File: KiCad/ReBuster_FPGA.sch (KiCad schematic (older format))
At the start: 28 parts, among them U1 10M02SCU169, U2 LM1117-3.3

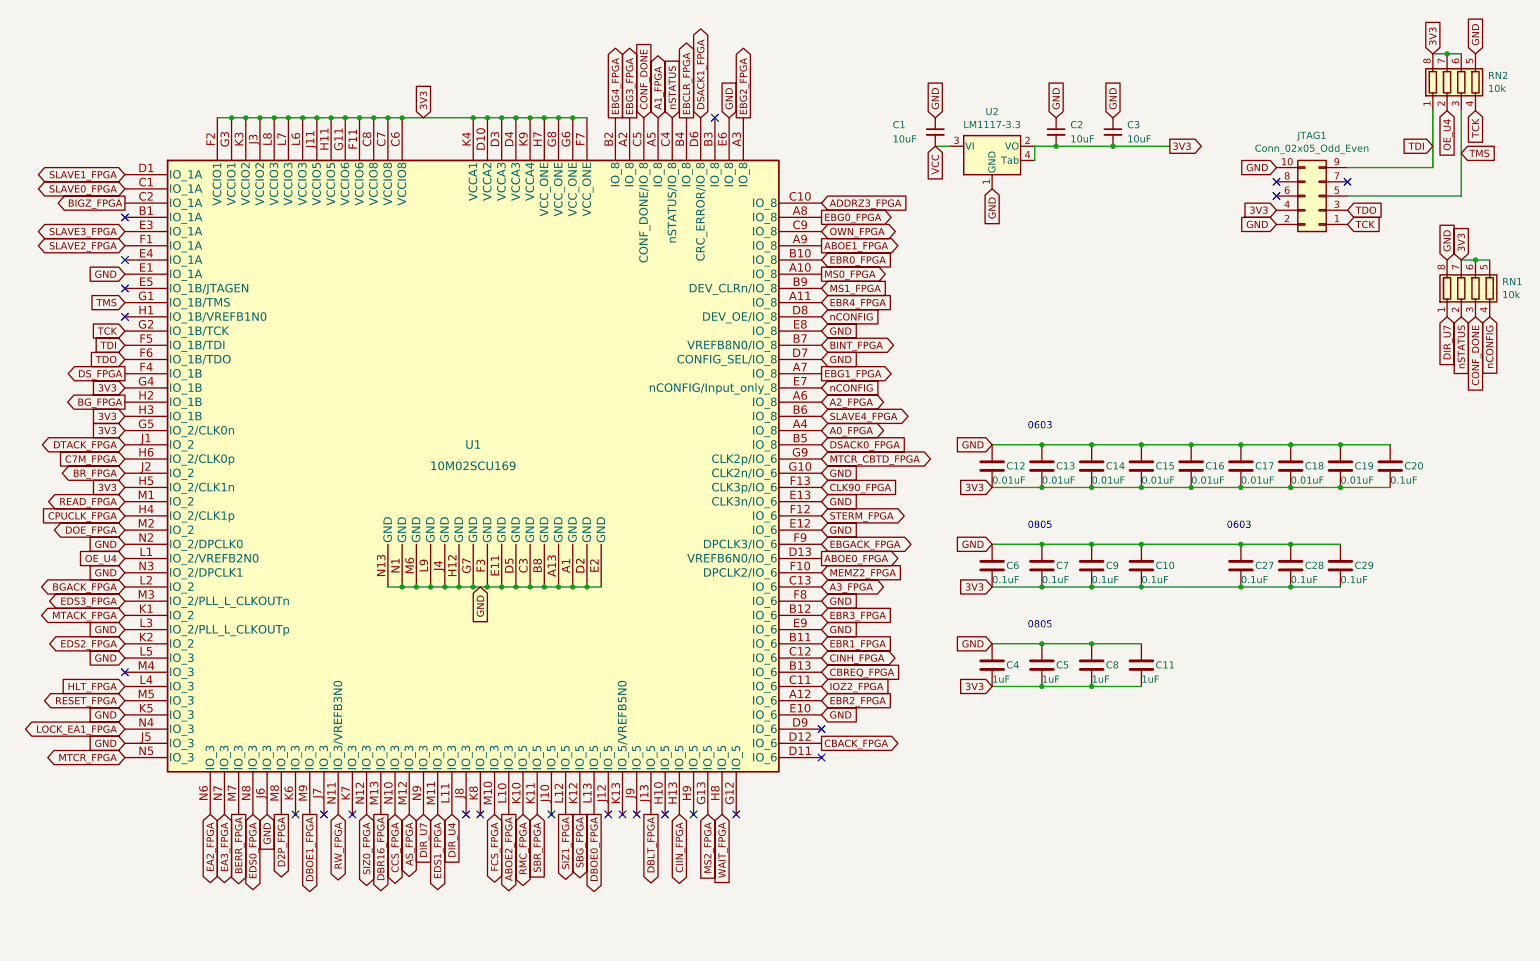
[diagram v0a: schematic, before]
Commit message: remove HLT-signal (not used) and put /DTACK signal there
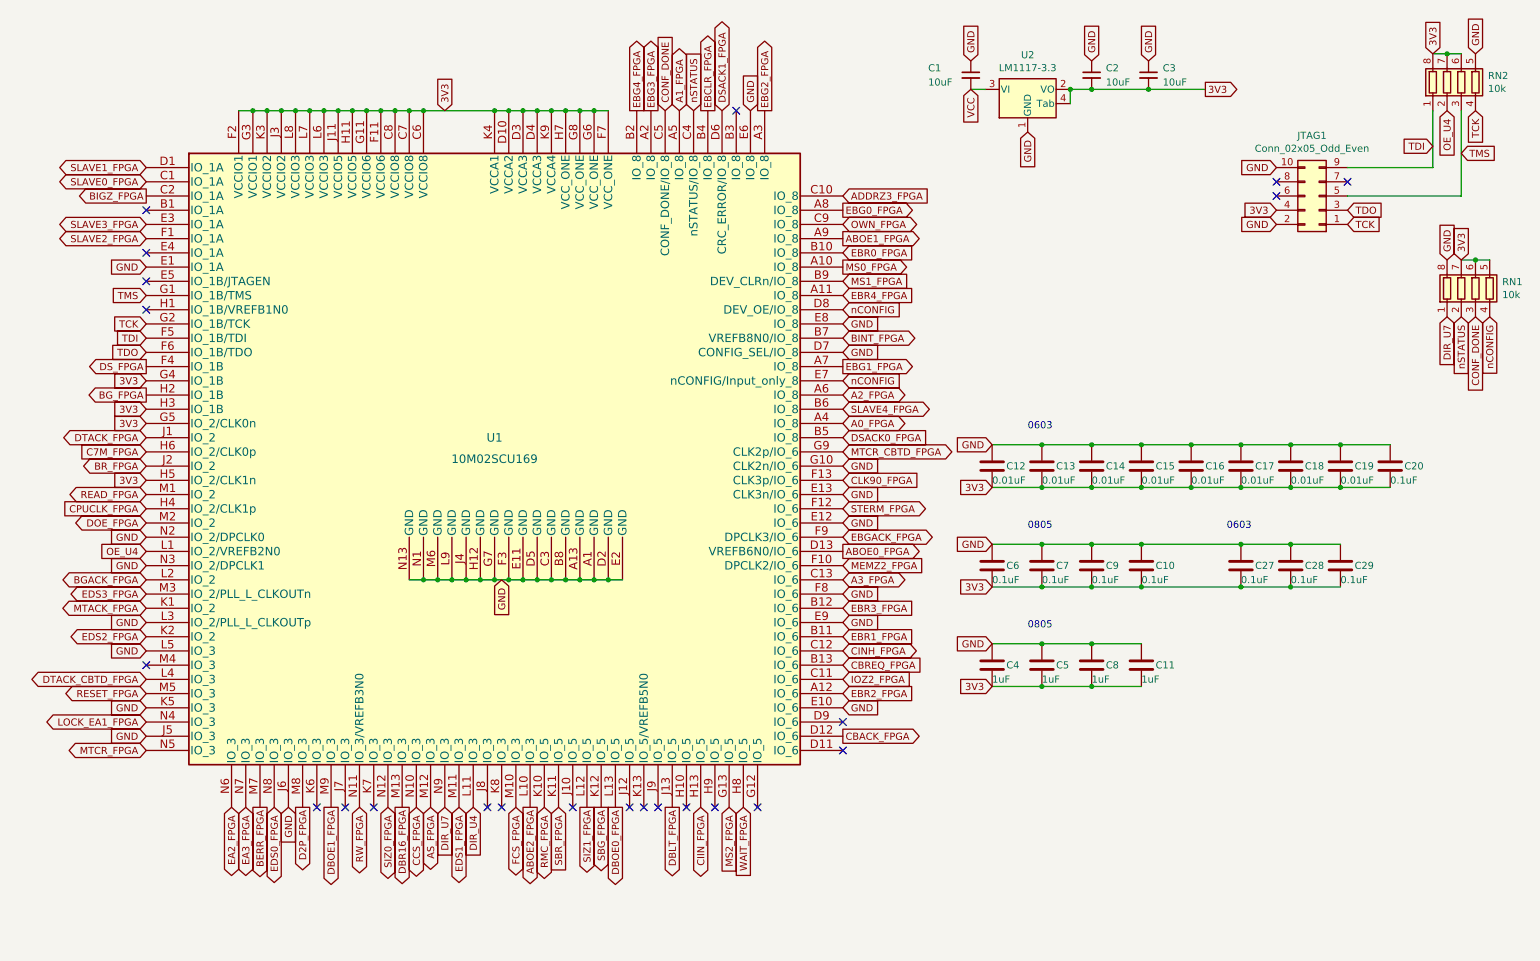
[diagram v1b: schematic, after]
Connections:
- net HLT_FPGA renamed DTACK_CBTD_FPGA
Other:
- moved on the sheet: C1, C2, C3, U1, U2

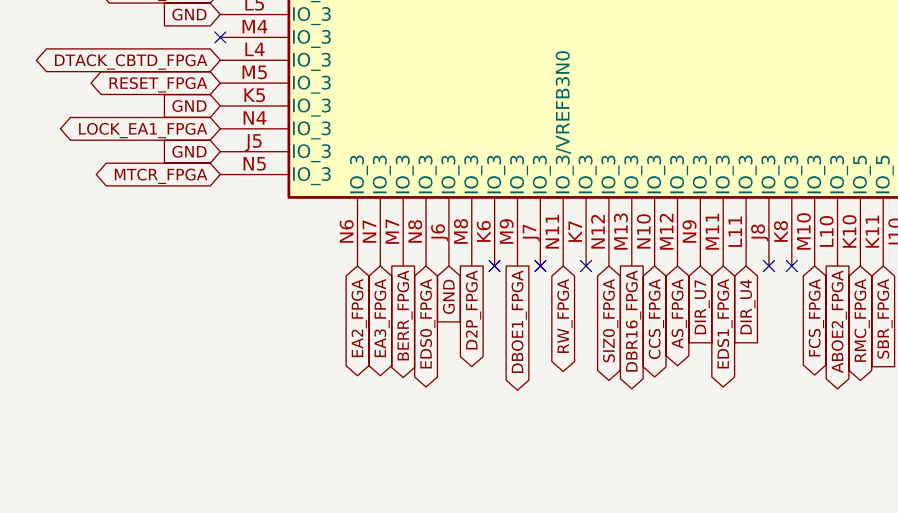
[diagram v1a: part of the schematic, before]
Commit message: Relocate EDS1 signal to replace MTCR's position (pin 9 and 40) in SN74LVC16T245
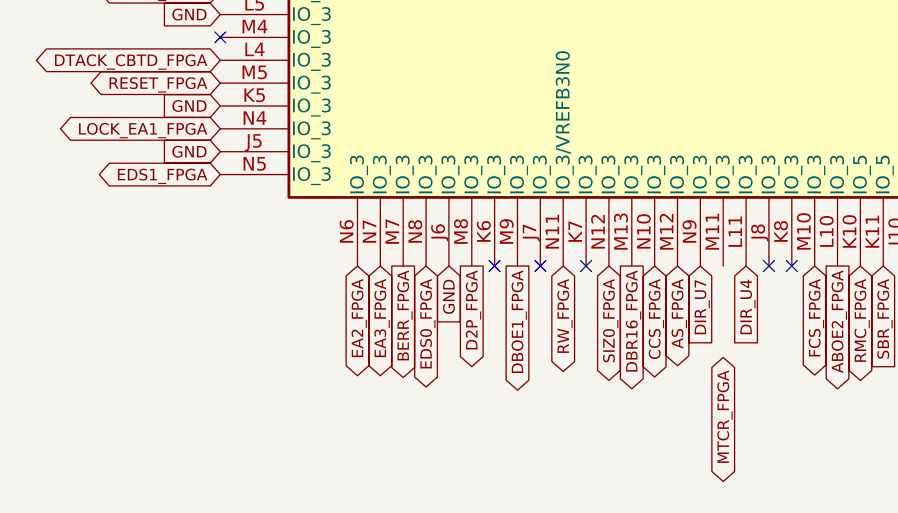
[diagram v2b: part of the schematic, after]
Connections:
- net EDS1_FPGA: now also U1.N5 (IO_3); no longer U1.M11 (IO_3)
- net MTCR_FPGA: no longer U1.N5 (IO_3)
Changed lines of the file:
@@
 Text GLabel 6200 3050 2    50   Output ~ 0
 EBG1_FPGA
-Text GLabel 3500 6150 3    50   BiDi ~ 0
+Text GLabel 1300 5750 0    50   BiDi ~ 0
 EDS1_FPGA
 Text GLabel 3900 6150 3    50   BiDi ~ 0
@@
 Text GLabel 5400 6150 3    50   Input ~ 0
 MS2_FPGA
-Text GLabel 1300 5750 0    50   BiDi ~ 0
+Text GLabel 3500 6550 3    50   BiDi ~ 0
 MTCR_FPGA
 Text GLabel 6200 5050 2    50   BiDi ~ 0

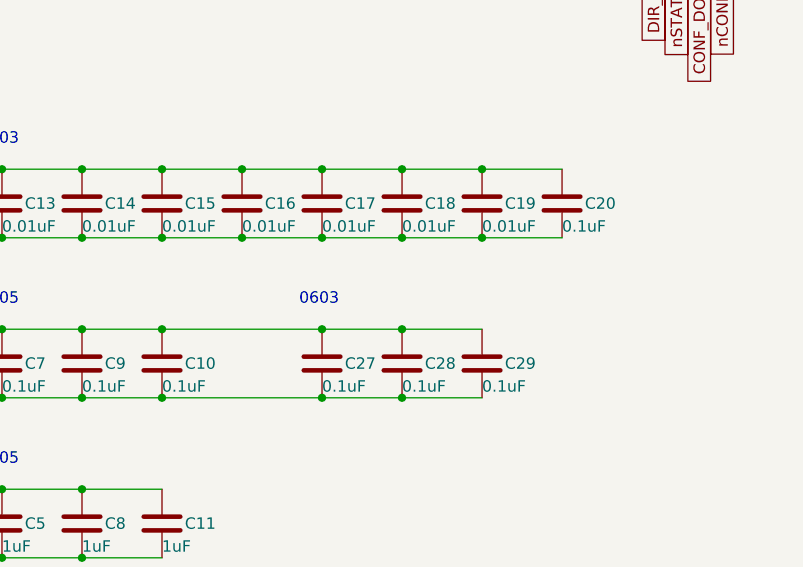
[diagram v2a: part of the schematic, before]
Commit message: Replace SN74LVC16T245DGVR with SN74LVC16245ADGVR and fix caps C24,C25 to instead be connected to 3V3
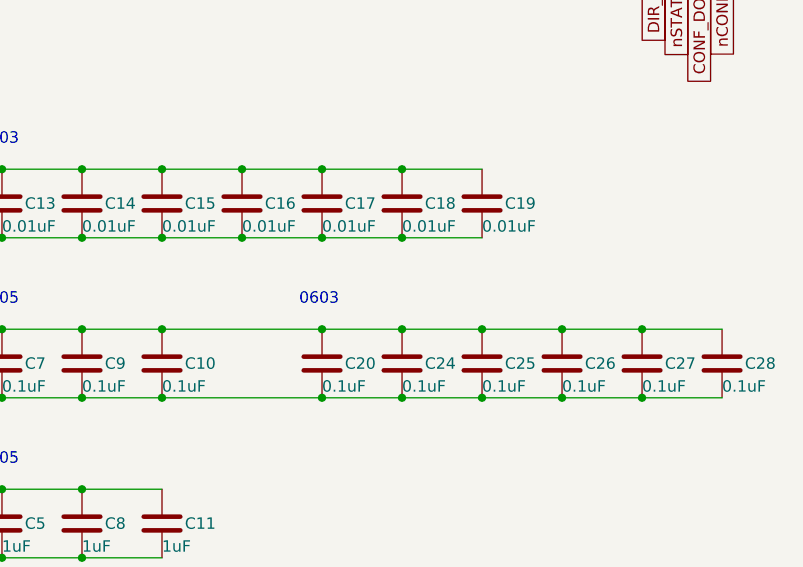
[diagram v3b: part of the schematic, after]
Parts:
- added C24, C25: 0.1uF, ReBuster:C_0603_1608Metric_Pad1.05x0.95mm_HandSolder_extended, symbol Device:C
- renumbered C27 to C26, C28 to C27, C29 to C28
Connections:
- net 3V3: now also C24.2, C25.2
- net GND: now also C24.1, C25.1
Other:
- moved on the sheet: C20, C26, C27, C28
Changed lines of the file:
@@
 L Device:C C?
 U 1 1 60CC8EF6
-P 10050 3750
+P 9000 4450
 AR Path="/60CC8EF6" Ref="C?"  Part="1"
 AR Path="/608A10F5/60CC8EF6" Ref="C20"  Part="1"
-F 0 "C20" H 10150 3750 50  0000 L CNN
-F 1 "0.1uF" H 10050 3650 50  0000 L CNN
-F 2 "Capacitor_SMD:C_0603_1608Metric_Pad1.05x0.95mm_HandSolder" H 10088 3600 50  0001 C CNN
-F 3 "~" H 10050 3750 50  0001 C CNN
-	1    10050 3750
+F 0 "C20" H 9100 4450 50  0000 L CNN
+F 1 "0.1uF" H 9000 4350 50  0000 L CNN
+F 2 "Capacitor_SMD:C_0603_1608Metric_Pad1.05x0.95mm_HandSolder" H 9038 4300 50  0001 C CNN
+F 3 "~" H 9000 4450 50  0001 C CNN
+	1    9000 4450
 	1    0    0    -1
 $EndComp
@@
 $EndComp
 Wire Wire Line
-	9700 3900 10050 3900
-Connection ~ 9700 3900
-Wire Wire Line
 	7250 3900 7600 3900
 Wire Wire Line
@@
 Wire Wire Line
 	9000 3600 9350 3600
-Wire Wire Line
-	10050 3600 9700 3600
-Connection ~ 9700 3600
 Wire Wire Line
 	8300 3900 8650 3900
@@
 L Device:C C?
 U 1 1 69ED3EAA
-P 9000 4450
+P 10050 4450
 AR Path="/69ED3EAA" Ref="C?"  Part="1"
-AR Path="/608A10F5/69ED3EAA" Ref="C27"  Part="1"
-F 0 "C27" H 9100 4450 50  0000 L CNN
-F 1 "0.1uF" H 9000 4350 50  0000 L CNN
-F 2 "Capacitor_SMD:C_0603_1608Metric_Pad1.08x0.95mm_HandSolder" H 9038 4300 50  0001 C CNN
-F 3 "~" H 9000 4450 50  0001 C CNN
-	1    9000 4450
+AR Path="/608A10F5/69ED3EAA" Ref="C26"  Part="1"
+F 0 "C26" H 10150 4450 50  0000 L CNN
+F 1 "0.1uF" H 10050 4350 50  0000 L CNN
+F 2 "Capacitor_SMD:C_0603_1608Metric_Pad1.08x0.95mm_HandSolder" H 10088 4300 50  0001 C CNN
+F 3 "~" H 10050 4450 50  0001 C CNN
+	1    10050 4450
 	1    0    0    -1
 $EndComp
@@
 0603
 Wire Wire Line
-	8300 4300 9000 4300
-Connection ~ 8300 4300
-Wire Wire Line
-	9000 4600 8300 4600
-Connection ~ 8300 4600
+	9350 4300 9700 4300
+Wire Wire Line
+	10050 4600 9700 4600
 $Comp
 L Device:C C?
 U 1 1 69EDC81C
-P 9350 4450
+P 10400 4450
 AR Path="/69EDC81C" Ref="C?"  Part="1"
-AR Path="/608A10F5/69EDC81C" Ref="C28"  Part="1"
-F 0 "C28" H 9450 4450 50  0000 L CNN
-F 1 "0.1uF" H 9350 4350 50  0000 L CNN
-F 2 "Capacitor_SMD:C_0603_1608Metric_Pad1.08x0.95mm_HandSolder" H 9388 4300 50  0001 C CNN
-F 3 "~" H 9350 4450 50  0001 C CNN
-	1    9350 4450
-	1    0    0    -1
-$EndComp
-Wire Wire Line
-	9000 4300 9350 4300
-Connection ~ 9000 4300
-Wire Wire Line
-	9000 4600 9350 4600
-Connection ~ 9000 4600
+AR Path="/608A10F5/69EDC81C" Ref="C27"  Part="1"
+F 0 "C27" H 10500 4450 50  0000 L CNN
+F 1 "0.1uF" H 10400 4350 50  0000 L CNN
+F 2 "Capacitor_SMD:C_0603_1608Metric_Pad1.08x0.95mm_HandSolder" H 10438 4300 50  0001 C CNN
+F 3 "~" H 10400 4450 50  0001 C CNN
+	1    10400 4450
+	1    0    0    -1
+$EndComp
+Wire Wire Line
+	10050 4300 10400 4300
+Connection ~ 10050 4300
+Wire Wire Line
+	10050 4600 10400 4600
+Connection ~ 10050 4600
 $Comp
 L Device:C C?
 U 1 1 69EF6B6A
-P 9700 4450
+P 10750 4450
 AR Path="/69EF6B6A" Ref="C?"  Part="1"
-AR Path="/608A10F5/69EF6B6A" Ref="C29"  Part="1"
-F 0 "C29" H 9800 4450 50  0000 L CNN
-F 1 "0.1uF" H 9700 4350 50  0000 L CNN
-F 2 "ReBuster:C_0603_1608Metric_Pad1.05x0.95mm_HandSolder_extended" H 9738 4300 50  0001 C CNN
-F 3 "~" H 9700 4450 50  0001 C CNN
-	1    9700 4450
-	1    0    0    -1
-$EndComp
-Wire Wire Line
-	9350 4300 9700 4300
-Connection ~ 9350 4300
-Wire Wire Line
-	9350 4600 9700 4600
-Connection ~ 9350 4600
+AR Path="/608A10F5/69EF6B6A" Ref="C28"  Part="1"
+F 0 "C28" H 10850 4450 50  0000 L CNN
+F 1 "0.1uF" H 10750 4350 50  0000 L CNN
+F 2 "ReBuster:C_0603_1608Metric_Pad1.05x0.95mm_HandSolder_extended" H 10788 4300 50  0001 C CNN
+F 3 "~" H 10750 4450 50  0001 C CNN
+	1    10750 4450
+	1    0    0    -1
+$EndComp
+Wire Wire Line
+	10400 4300 10750 4300
+Connection ~ 10400 4300
+Wire Wire Line
+	10400 4600 10750 4600
+Connection ~ 10400 4600
 Text GLabel 6200 3650 2    50   BiDi ~ 0
 MTCR_CBTD_FPGA
@@
 DTACK_CBTD_FPGA
 Connection ~ 7800 1100
+$Comp
+L Device:C C?
+U 1 1 6A084E8F
+P 9700 4450
+AR Path="/6A084E8F" Ref="C?"  Part="1"
+AR Path="/608A10F5/6A084E8F" Ref="C25"  Part="1"
+F 0 "C25" H 9800 4450 50  0000 L CNN
+F 1 "0.1uF" H 9700 4350 50  0000 L CNN
+F 2 "ReBuster:C_0603_1608Metric_Pad1.05x0.95mm_HandSolder_extended" H 9738 4300 50  0001 C CNN
+F 3 "~" H 9700 4450 50  0001 C CNN
+	1    9700 4450
+	1    0    0    -1
+$EndComp
+$Comp
+L Device:C C?
+U 1 1 6A084E95
+P 9350 4450
+AR Path="/6A084E95" Ref="C?"  Part="1"
+AR Path="/608A10F5/6A084E95" Ref="C24"  Part="1"
+F 0 "C24" H 9450 4450 50  0000 L CNN
+F 1 "0.1uF" H 9350 4350 50  0000 L CNN
+F 2 "ReBuster:C_0603_1608Metric_Pad1.05x0.95mm_HandSolder_extended" H 9388 4300 50  0001 C CNN
+F 3 "~" H 9350 4450 50  0001 C CNN
+	1    9350 4450
+	1    0    0    -1
+$EndComp
+Wire Wire Line
+	9700 4600 9350 4600
+Connection ~ 9700 4300
+Wire Wire Line
+	9700 4300 10050 4300
+Connection ~ 9700 4600
+Wire Wire Line
+	8300 4300 9000 4300
+Connection ~ 8300 4300
+Connection ~ 9350 4300
+Connection ~ 9000 4300
+Wire Wire Line
+	9000 4300 9350 4300
+Wire Wire Line
+	8300 4600 9000 4600
+Connection ~ 8300 4600
+Connection ~ 9350 4600
+Connection ~ 9000 4600
+Wire Wire Line
+	9000 4600 9350 4600
 $EndSCHEMATC
